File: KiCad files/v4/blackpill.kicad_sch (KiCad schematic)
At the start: 2 parts, among them J8 Conn_01x20_Socket, J9 Conn_01x20_Socket

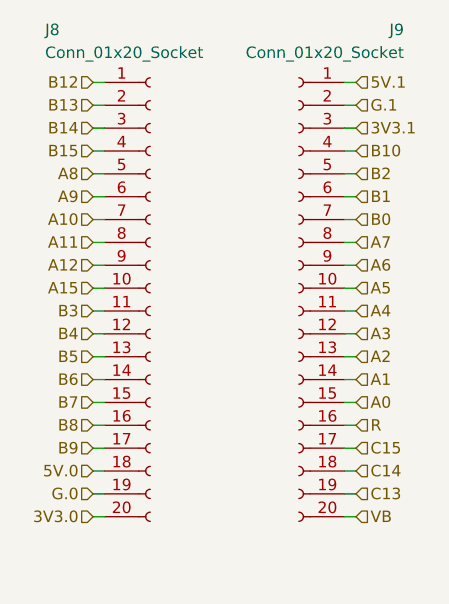
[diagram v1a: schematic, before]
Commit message: Generated output files for docs. Removed old fabrication files.
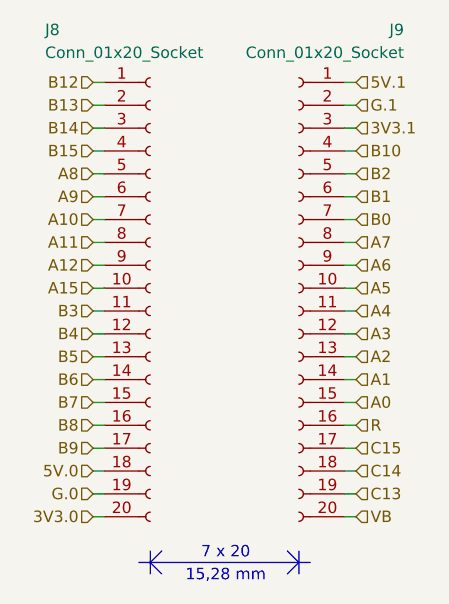
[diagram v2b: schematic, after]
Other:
- note added: "15,28 mm"
- note added: "7 x 20"
